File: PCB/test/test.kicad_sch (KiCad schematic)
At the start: 54 parts, among them CN5 UFL, SW2 MLL1200S_TE, U1 STM32WBxx_QFN48, U2 USBLC6-2SC6, U3 LD3985M33R, X1 NX2016_32MHz, X2 NX2012_32K768Hz

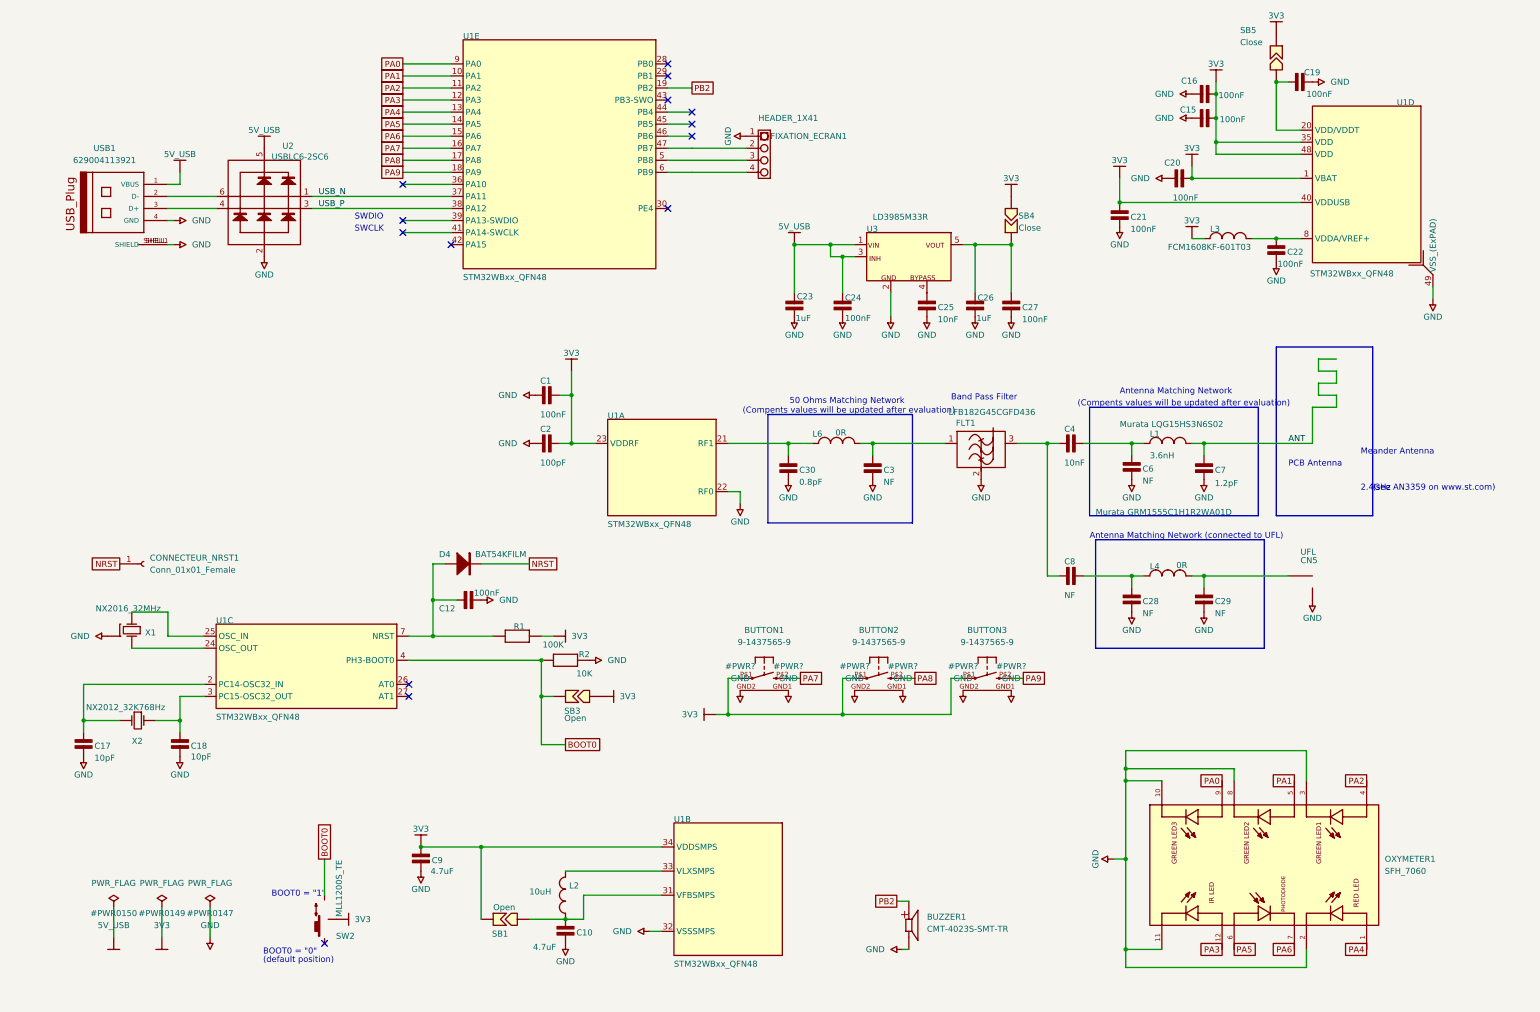
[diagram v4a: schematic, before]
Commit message: suppression du bouton boot + pcb usb
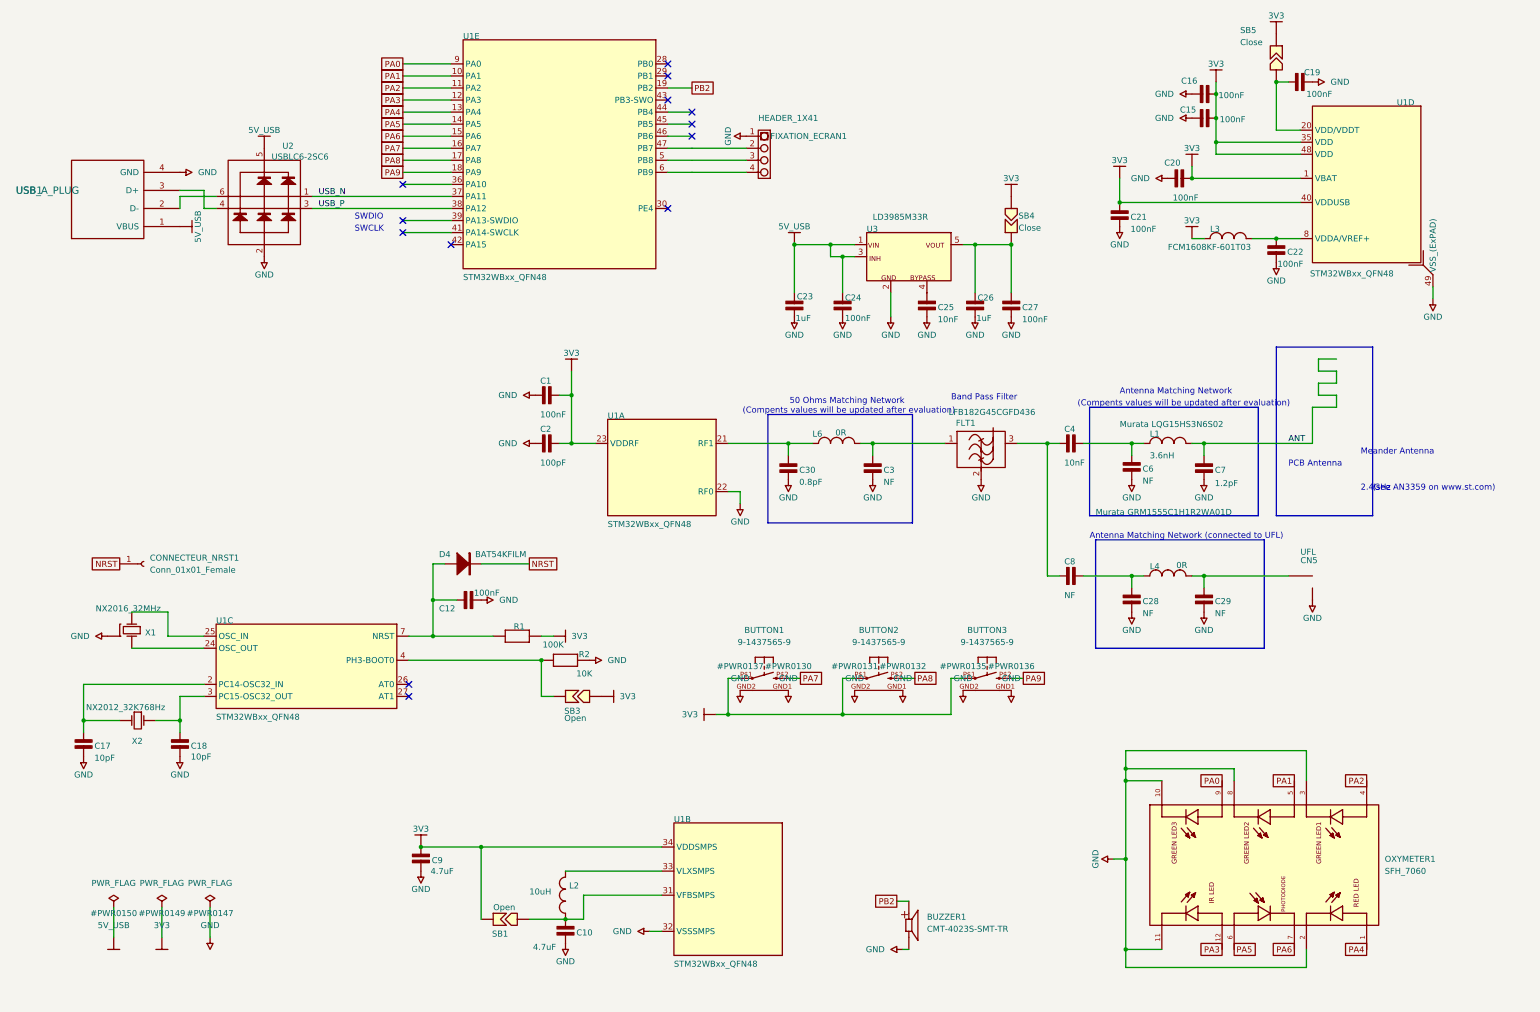
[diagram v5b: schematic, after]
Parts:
- removed SW2: MLL1200S_TE, Library:MLL1200S_TE, symbol test-altium-import:3_mirrored_MLL1200S_TE
- removed USB1: 629004113921, 629004113921:629004113921, symbol 629004113921:629004113921
- added USB1: USB_A_PLUG, symbol armory:USB_A_PLUG
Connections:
- net 5V_USB: now also USB1.1 (VBUS)
- net GND: now also USB1.4 (GND)
- net at U2.4: now also USB1.3 (D+)
- net at U2.6: now also USB1.2 (D-)
- net BOOT0: no longer names the net of R2.1, SB3.2, U1.4 (PH3-BOOT0)
- no-connect marks 14 -> 13
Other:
- note removed: "(default position)"
- note removed: "BOOT0 = "0""
- note removed: "BOOT0 = "1""

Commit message: changement oxymètre
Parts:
- removed OXYMETER1: SFH_7060, SFH_7060:XDCR_SFH_7060, symbol SFH_7060:SFH_7060
- added OXY1: SFH_7072, XDCR_SFH_7060, symbol SFH_7072:SFH_7072
- USB1: footprint (none) -> Connector_USB:usb-PCB
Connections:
- net GND: now also OXY1.1, OXY1.12, OXY1.6, OXY1.8, OXY1.9
- net PA0: now also OXY1.2
- net PA1: now also OXY1.4
- net PA2: now also OXY1.5
- net PA3: now also OXY1.3
- net PA4: now also OXY1.7
- net PA5: now also OXY1.10
- net PA6: now also OXY1.11

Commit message: beaucoup de changements
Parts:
- removed BUTTON1, BUTTON2, BUTTON3: 9-1437565-9, FSMRACD, symbol 9-1437565-9:9-1437565-9
- removed BUZZER1: CMT-4023S-SMT-TR, CMT-4023S-SMT-TR:CUI_CMT-4023S-SMT-TR, symbol CMT-4023S-SMT-TR:CMT-4023S-SMT-TR
- removed C28, C29: NF, Library:0402_CAP_NPOL, symbol test-altium-import:0_CAP_NPOL
- removed C8: NF, Library:0402_CAP_NPOL, symbol test-altium-import:1_CAP_NPOL
- removed CN5: UFL, Library:UFL, symbol test-altium-import:0_mirrored_UFL
- removed L4: 0R, Library:0402_COIL, symbol test-altium-import:1_INDUCTOR_SMD_STDL
- removed SB3: Open, Library:SB-tiny, symbol test-altium-import:0_Strap2
- added BATTERY1: BAT-HLD-002-SMT, BAT_BAT-HLD-002-SMT, symbol BAT-HLD-002-SMT:BAT-HLD-002-SMT
- added BOOT1: Conn_01x02_Male, Connector_PinHeader_2.54mm:PinHeader_1x02_P2.54mm_Vertical, symbol Connector:Conn_01x02_Male
- added BUZZER1: KSSG13J12-N, XDCR_KSSG13J12-N, symbol KSSG13J12-N:KSSG13J12-N
- added JOYSTICK1: JS1400AFQ, SW_JS1400AFQ, symbol JS1400AFQ:JS1400AFQ
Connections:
- net 3V3: now also BOOT1.2 (Pin_2), JOYSTICK1.1, JOYSTICK1.2, JOYSTICK1.3
- net 5V_USB: now also BATTERY1.P1, BATTERY1.P2
- net GND: now also BATTERY1.N, BUZZER1.N, JOYSTICK1.G1 (GND), JOYSTICK1.G2 (GND)
- net PA7: now also JOYSTICK1.4
- net PA8: now also JOYSTICK1.5
- net PA9: now also JOYSTICK1.6
- net PB2: now also BUZZER1.P
- net at R2.1, U1.4 (PH3-BOOT0): now also BOOT1.1 (Pin_1)
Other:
- note removed: "Antenna Matching Network (connected to UFL)"

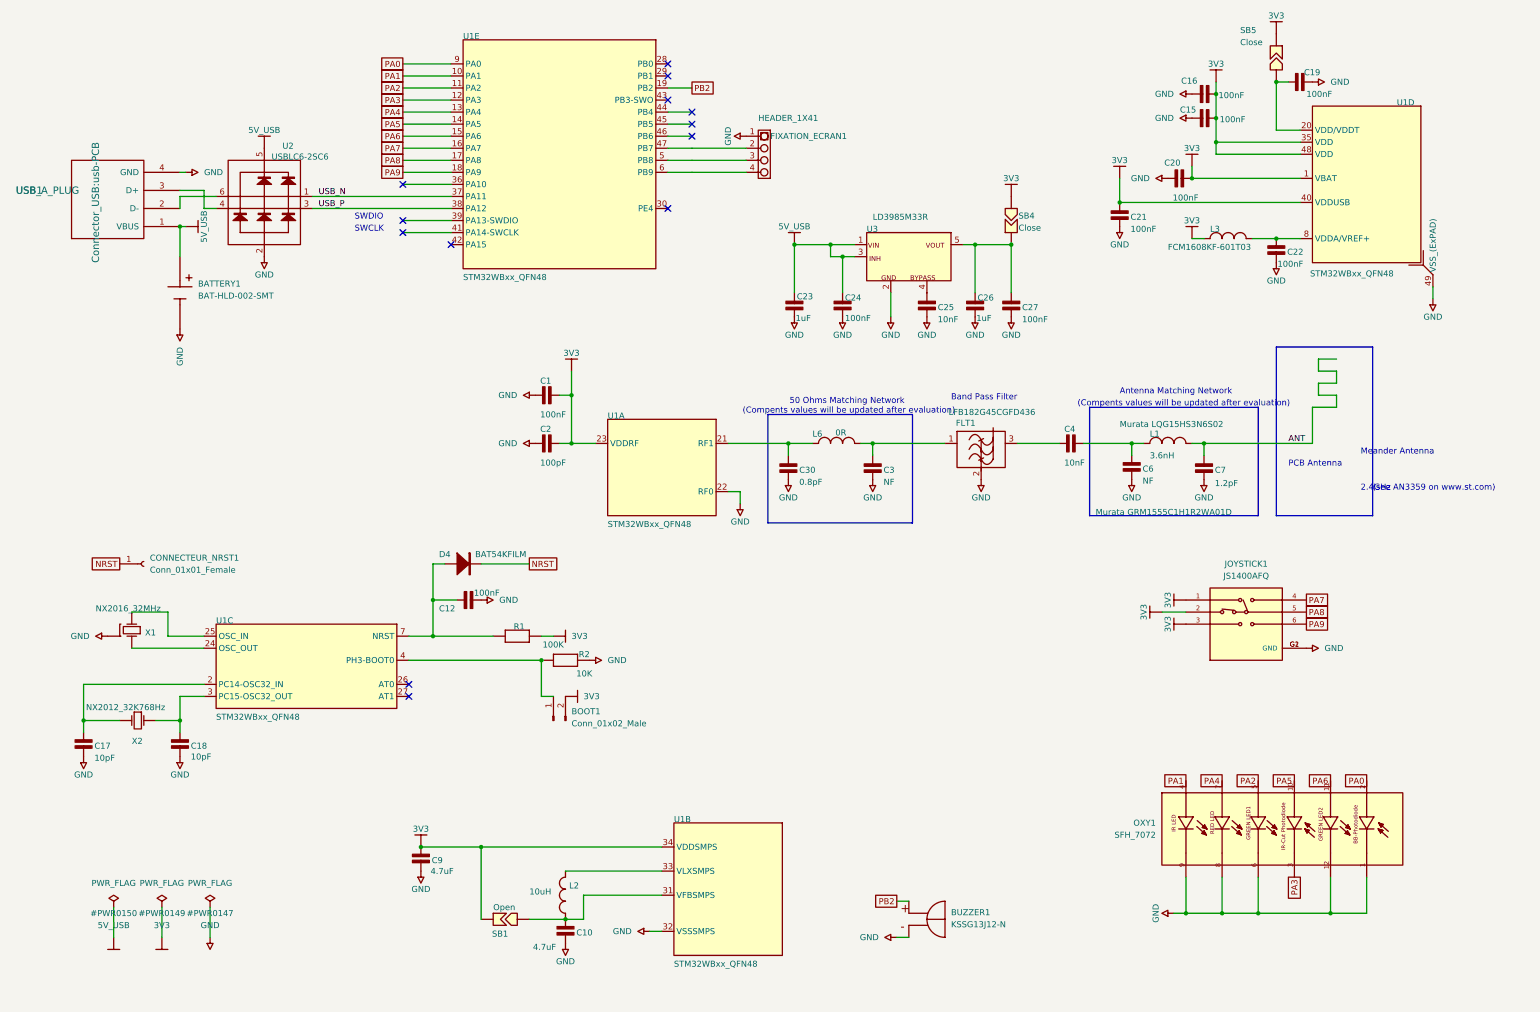
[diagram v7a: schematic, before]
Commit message: ajout ampliop capteur, reste UVNC et 10x pin header
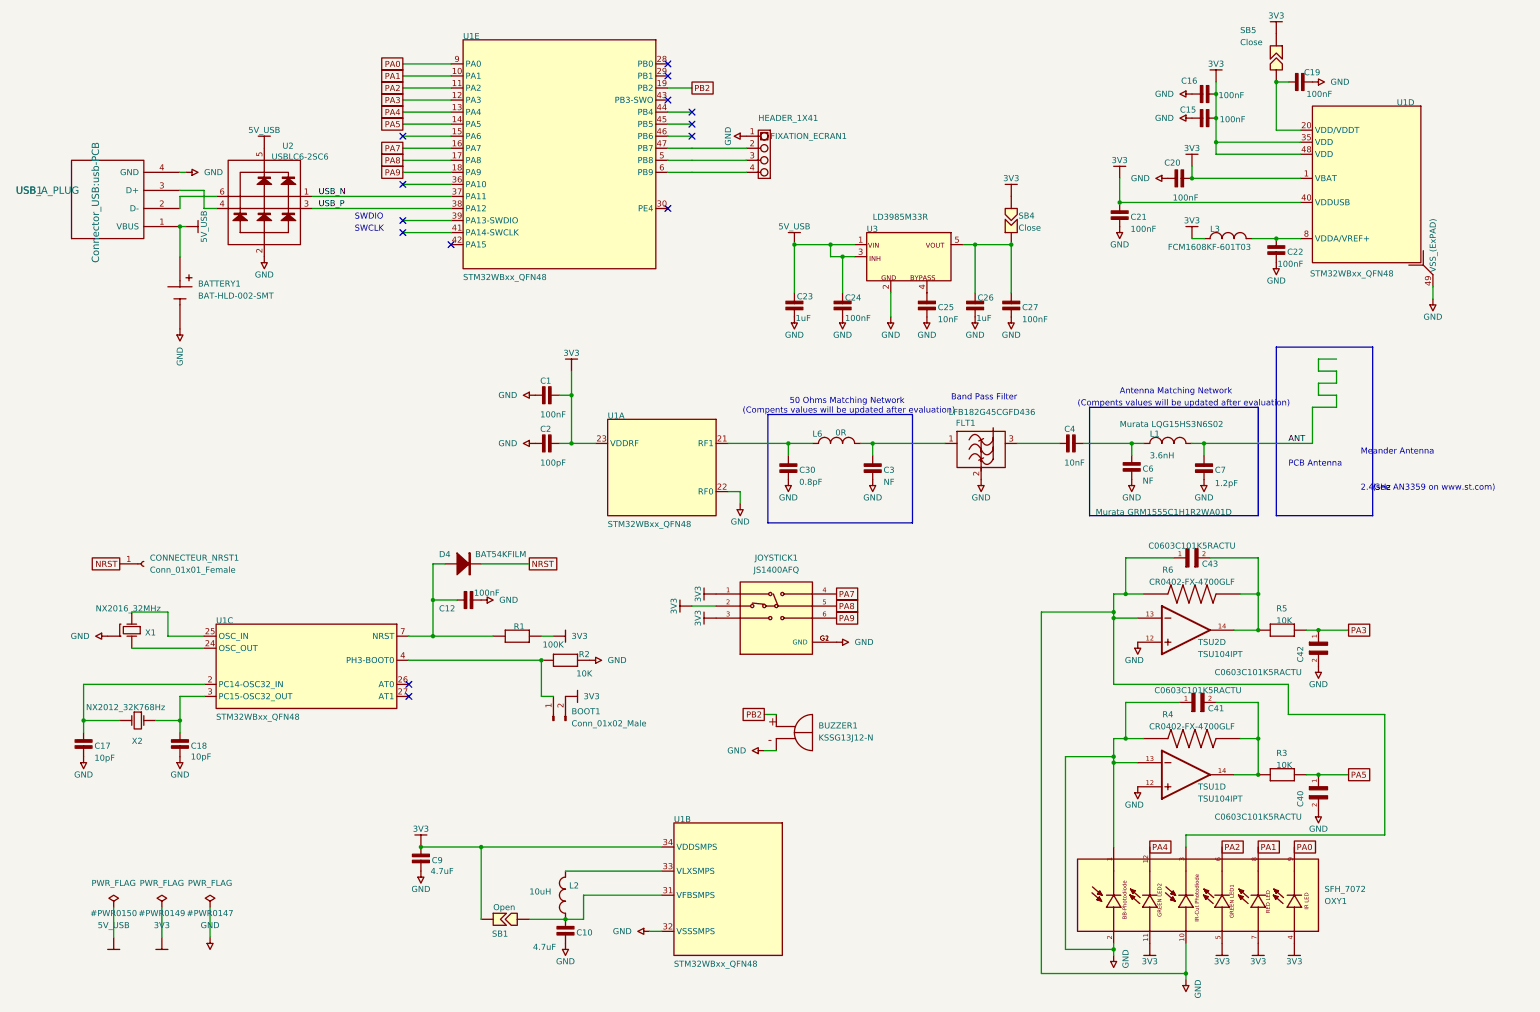
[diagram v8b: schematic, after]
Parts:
- added C40, C41, C42, C43: C0603C101K5RACTU, CAPC1608X87N, symbol C0603C101K5RACTU:C0603C101K5RACTU
- added R3, R5: 10K, Library:0402_RES, symbol test-altium-import:0_RES
- added R4, R6: CR0402-FX-4700GLF, RESC1005X40N, symbol CR0402-FX-4700GLF:CR0402-FX-4700GLF
- added TSU1, TSU2: TSU104IPT, SOP65P640X120-14N, symbol TSU104IPT:TSU104IPT
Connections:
- net 3V3: now also OXY1.11, OXY1.4, OXY1.5, OXY1.7
- net GND: now also OXY1.10, OXY1.2, OXY1.3, C40.2, C41.1, C42.2, C43.1, R4.1, R6.1, TSU1.12, TSU1.13, TSU2.12, TSU2.13; no longer OXY1.12, OXY1.6, OXY1.8, OXY1.9
- net PA0: now also OXY1.9; no longer OXY1.2
- net PA1: now also OXY1.8; no longer OXY1.4
- net PA2: now also OXY1.6; no longer OXY1.5
- net PA3: now also C42.1, R5.2; no longer OXY1.3
- net PA4: now also OXY1.12; no longer OXY1.7
- net PA5: now also C40.1, R3.2; no longer OXY1.10
- net PA6: no longer names the net of U1.15 (PA6)
- net PA6: no longer OXY1.11
- new net: C43.2, R5.1, R6.2, TSU2.14
- new net: C41.2, R3.1, R4.2, TSU1.14
- no-connect marks 13 -> 14
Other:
- moved on the sheet: BUZZER1, JOYSTICK1, OXY1
